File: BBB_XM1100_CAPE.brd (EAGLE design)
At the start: 54.6 x 71.8 mm, 24 parts, among them U2 MIC5225-3.3

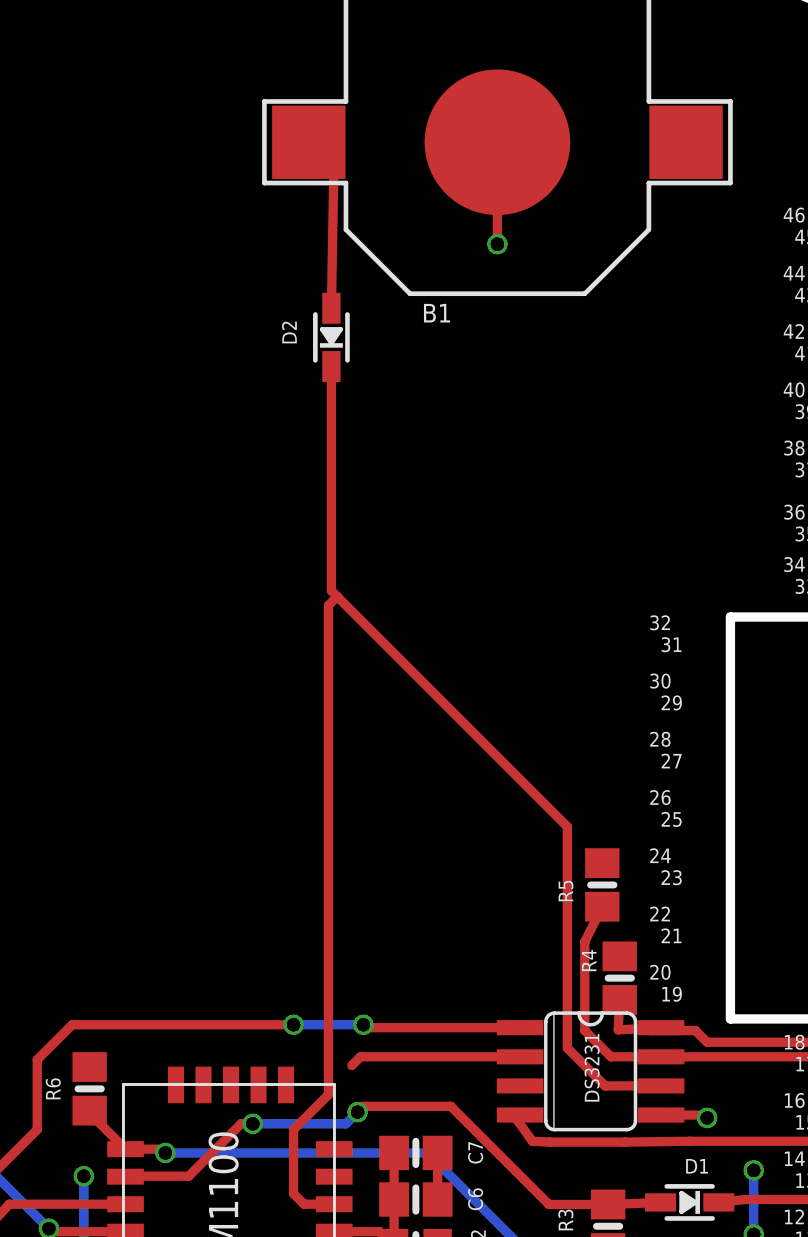
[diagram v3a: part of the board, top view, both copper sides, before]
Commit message: added eeprom to XM1100 cape
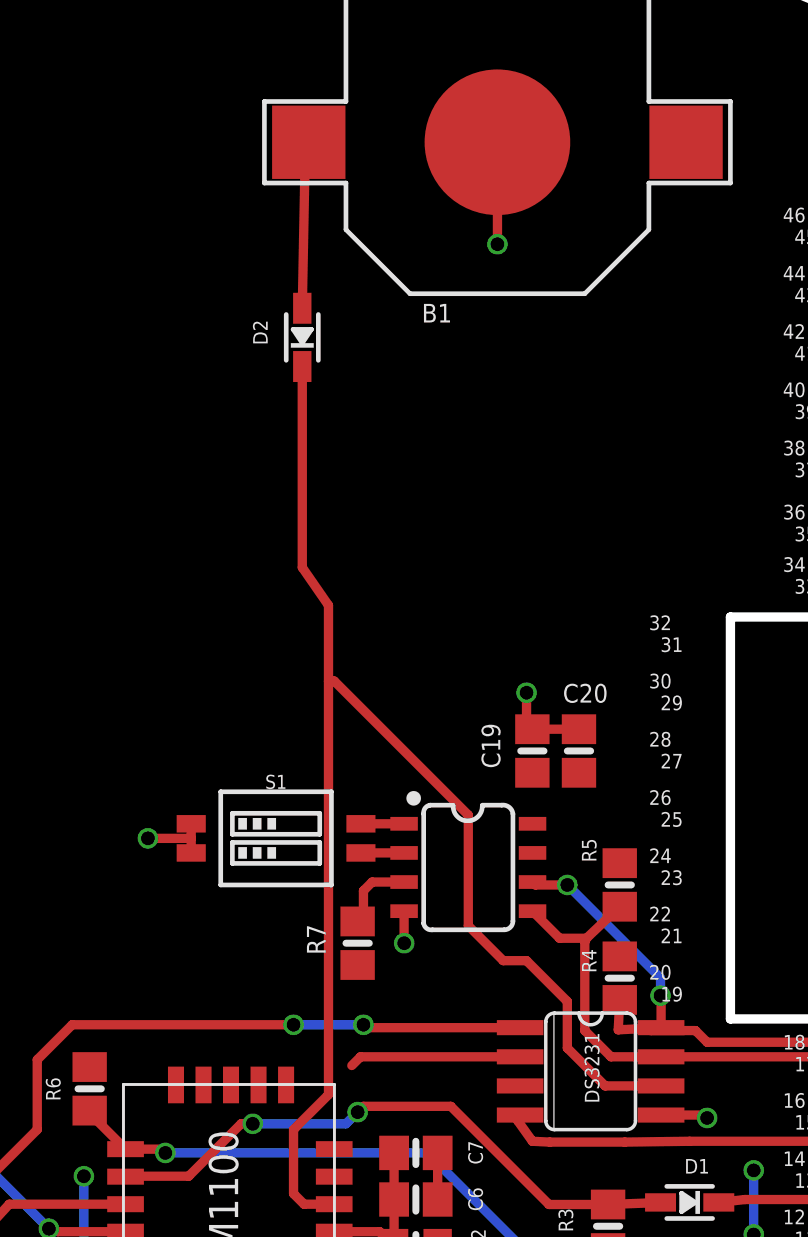
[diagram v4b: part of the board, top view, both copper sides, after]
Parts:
- added C19: 0.1uF, microbuilder:0805-NO
- added C20: 10uF, microbuilder:0805-NO
- added R7: 10K, microbuilder:0805-NO
- added S1: DIP-02-SMD-50MIL, SparkFun-Switches:DIPSWITCH-02-50MIL
- added U1: 24LC256, SparkFun-IC-Memory:SO08
- moved D2 1.27 mm to (27.8, 56.1)
- moved R5 0.76 mm to (41.7, 32.3)
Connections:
- new net N$13: R7.2, U1.3
- new net N$15: S1.3, U1.2
- new net N$16: S1.4, U1.1
- net 3.3V: now also C19.1, C20.1, R7.1, U1.8
- net GND: now also C19.2, C20.2, S1.1, S1.2, U1.4
- net SCL: now also U1.6
- net SDA: now also U1.5
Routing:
- net SCL: track 17.2 -> 26.6 mm, vias 0 -> 2
- net GND: track 17.2 -> 25.5 mm, vias 15 -> 18
- net N$13: track 0.00 -> 3.37 mm
- net SDA: track 18.9 -> 22.2 mm
- net VBACKUP: track 67.5 -> 64.9 mm
- net N$16: track 0.00 -> 1.88 mm
- net N$15: track 0.00 -> 1.88 mm
- net N$1: track 8.35 -> 7.26 mm
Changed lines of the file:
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@@
 </element>
 <element name="U$20" library="microbuilder" package="U.FL" value="U.FL" x="18.288" y="8.255" smashed="yes"/>
-<element name="D2" library="microbuilder" package="SOD-323" value="CUS520" x="29.083" y="56.134" smashed="yes" rot="R90">
-<attribute name="NAME" x="27.575" y="55.796" size="0.635" layer="25" rot="R90"/>
+<element name="D2" library="microbuilder" package="SOD-323" value="CUS520" x="27.813" y="56.134" smashed="yes" rot="R90">
+<attribute name="NAME" x="26.305" y="55.796" size="0.635" layer="25" rot="R90"/>
 </element>
 <element name="U$15" library="adafruit" package="BEAGLEBONE_SHIELD" value="BEAGLEBONE_OUTLINE" x="2.794" y="-14.478" smashed="yes"/>
@@
 <attribute name="NAME" x="40.005" y="29.464" size="0.635" layer="25" rot="R270"/>
 </element>
-<element name="R5" library="microbuilder" package="0805-NO" value="10K" x="40.894" y="32.258" smashed="yes" rot="R270">
-<attribute name="NAME" x="38.989" y="32.512" size="0.635" layer="25" rot="R270"/>
+<element name="R5" library="microbuilder" package="0805-NO" value="10K" x="41.656" y="32.258" smashed="yes" rot="R270">
+<attribute name="NAME" x="40.005" y="34.29" size="0.635" layer="25" rot="R270"/>
 </element>
 <element name="DS3231" library="tuckerLib" package="SO08" value="DS3231M-8PIN" x="40.386" y="24.13" smashed="yes" rot="R270">
@@
 <element name="R6" library="microbuilder" package="0805-NO" value="10K" x="18.542" y="23.368" smashed="yes" rot="R270">
 <attribute name="NAME" x="16.637" y="23.876" size="0.635" layer="25" rot="R270"/>
+</element>
+<element name="U1" library="SparkFun-IC-Memory" package="SO08" value="24LC256" x="35.052" y="33.02" smashed="yes" rot="R270">
+<attribute name="PROD_ID" value="IC-09714" x="44.45" y="33.02" size="1.778" layer="27" rot="R270" display="off"/>
+<attribute name="VALUE" x="35.306" y="32.766" size="0.6096" layer="27" font="vector" ratio="20" rot="R90" align="bottom-center"/>
+</element>
+<element name="S1" library="SparkFun-Switches" package="DIPSWITCH-02-50MIL" value="DIP-02-SMD-50MIL" x="26.67" y="34.29" smashed="yes" rot="R270">
+<attribute name="PROD_ID" value="SWCH-13215" x="28.956" y="40.386" size="1.778" layer="27" rot="R270" display="off"/>
+<attribute name="NAME" x="26.67" y="36.449" size="0.6096" layer="25" font="vector" ratio="20" align="bottom-center"/>
+</element>
+<element name="R7" library="microbuilder" package="0805-NO" value="10K" x="30.226" y="29.718" smashed="yes" rot="R90">
+<attribute name="NAME" x="28.829" y="29.21" size="0.8128" layer="25" ratio="18" rot="R90"/>
+</element>
+<element name="C19" library="microbuilder" package="0805-NO" value="0.1uF" x="37.846" y="38.1" smashed="yes" rot="R90">
+<attribute name="NAME" x="36.449" y="37.338" size="0.8128" layer="25" ratio="18" rot="R90"/>
+</element>
+<element name="C20" library="microbuilder" package="0805-NO" value="10uF" x="39.878" y="38.1" smashed="yes" rot="R90">
+<attribute name="NAME" x="41.148" y="41.021" size="0.8128" layer="25" ratio="18" rot="R180"/>
 </element>
 </elements>
@@
 <via x="36.322" y="60.198" extent="1-16" drill="0.6" shape="square"/>
 <wire x1="36.322" y1="60.198" x2="36.322" y2="64.643" width="0.4064" layer="1"/>
+<contactref element="S1" pad="1"/>
+<contactref element="S1" pad="2"/>
+<contactref element="U1" pad="4"/>
+<contactref element="C19" pad="2"/>
+<contactref element="C20" pad="2"/>
+<via x="21.082" y="34.29" extent="1-16" drill="0.6" shape="square"/>
+<via x="37.592" y="40.64" extent="1-16" drill="0.6" shape="square"/>
+<via x="32.258" y="29.718" extent="1-16" drill="0.6" shape="square"/>
+<wire x1="32.258" y1="29.718" x2="32.252" y2="29.724" width="0.4064" layer="1"/>
+<wire x1="32.252" y1="29.724" x2="32.252" y2="31.115" width="0.4064" layer="1"/>
+<wire x1="39.878" y1="39.05" x2="37.846" y2="39.05" width="0.4064" layer="1"/>
+<wire x1="37.846" y1="39.05" x2="37.592" y2="39.304" width="0.4064" layer="1"/>
+<wire x1="37.592" y1="39.304" x2="37.592" y2="40.64" width="0.4064" layer="1"/>
+<wire x1="22.97" y1="33.655" x2="22.97" y2="34.29" width="0.4064" layer="1"/>
+<wire x1="22.97" y1="34.29" x2="22.97" y2="34.925" width="0.4064" layer="1"/>
+<wire x1="21.082" y1="34.29" x2="22.97" y2="34.29" width="0.4064" layer="1"/>
 <wire x1="29.206" y1="15.938" x2="29.206" y2="19.538" width="0" layer="19" extent="1-1"/>
 <wire x1="25.906" y1="13.138" x2="27.106" y2="13.138" width="0" layer="19" extent="1-1"/>
@@
 <via x="18.288" y="16.002" extent="1-16" drill="0.6" shape="square"/>
 <wire x1="18.288" y1="16.002" x2="18.288" y2="19.558" width="0.4064" layer="16"/>
+<contactref element="R7" pad="1"/>
+<contactref element="C19" pad="1"/>
+<contactref element="C20" pad="1"/>
+<contactref element="U1" pad="8"/>
 </signal>
 <signal name="ENABLE">
@@
 <wire x1="43.4594" y1="23.495" x2="41.021" y2="23.495" width="0.4064" layer="1"/>
 <wire x1="41.021" y1="23.495" x2="39.37" y2="25.146" width="0.4064" layer="1"/>
-<wire x1="39.37" y1="25.146" x2="39.37" y2="34.798" width="0.4064" layer="1"/>
-<wire x1="39.37" y1="34.798" x2="29.337" y2="44.831" width="0.4064" layer="1"/>
 <wire x1="29.206" y1="18.338" x2="27.89" y2="18.338" width="0.4064" layer="1"/>
 <wire x1="27.89" y1="18.338" x2="27.432" y2="18.796" width="0.4064" layer="1"/>
 <wire x1="27.432" y1="18.796" x2="27.432" y2="21.59" width="0.4064" layer="1"/>
 <wire x1="27.432" y1="21.59" x2="28.956" y2="23.114" width="0.4064" layer="1"/>
-<wire x1="28.956" y1="23.114" x2="28.956" y2="44.45" width="0.4064" layer="1"/>
-<wire x1="28.956" y1="44.45" x2="29.337" y2="44.831" width="0.4064" layer="1"/>
-<wire x1="29.083" y1="54.864" x2="29.083" y2="45.085" width="0.4064" layer="1"/>
-<wire x1="29.083" y1="45.085" x2="29.337" y2="44.831" width="0.4064" layer="1"/>
+<wire x1="28.956" y1="23.114" x2="28.956" y2="41.148" width="0.4064" layer="1"/>
+<wire x1="28.956" y1="41.148" x2="28.956" y2="44.45" width="0.4064" layer="1"/>
+<wire x1="28.956" y1="44.45" x2="27.813" y2="46.101" width="0.4064" layer="1"/>
+<wire x1="27.813" y1="54.864" x2="27.813" y2="46.101" width="0.4064" layer="1"/>
+<wire x1="39.37" y1="25.146" x2="39.37" y2="27.178" width="0.4064" layer="1"/>
+<wire x1="39.37" y1="27.178" x2="37.592" y2="28.956" width="0.4064" layer="1"/>
+<wire x1="37.592" y1="28.956" x2="36.576" y2="28.956" width="0.4064" layer="1"/>
+<wire x1="36.576" y1="28.956" x2="35.052" y2="30.48" width="0.4064" layer="1"/>
+<wire x1="35.052" y1="30.48" x2="35.052" y2="35.306" width="0.4064" layer="1"/>
+<wire x1="35.052" y1="35.306" x2="29.21" y2="41.148" width="0.4064" layer="1"/>
+<wire x1="29.21" y1="41.148" x2="28.956" y2="41.148" width="0.4064" layer="1"/>
 </signal>
 <signal name="TX">
@@
 <contactref element="D2" pad="A"/>
 <contactref element="B1" pad="+$1"/>
-<wire x1="28.0966" y1="64.643" x2="29.21" y2="64.643" width="0.4064" layer="1"/>
-<wire x1="29.21" y1="64.643" x2="29.083" y2="57.404" width="0.4064" layer="1"/>
+<wire x1="28.0966" y1="64.643" x2="27.94" y2="64.135" width="0.4064" layer="1"/>
+<wire x1="27.94" y1="64.135" x2="27.813" y2="57.404" width="0.4064" layer="1"/>
 </signal>
 <signal name="VDD_3V3EXP">
@@
 <wire x1="41.275" y1="24.765" x2="40.132" y2="25.908" width="0.4064" layer="1"/>
 <wire x1="40.132" y1="25.908" x2="40.132" y2="29.784" width="0.4064" layer="1"/>
-<wire x1="40.132" y1="29.784" x2="40.894" y2="31.308" width="0.4064" layer="1"/>
+<wire x1="40.132" y1="29.784" x2="40.2072" y2="29.9344" width="0.4064" layer="1"/>
+<contactref element="U1" pad="5"/>
+<wire x1="40.2072" y1="29.9344" x2="41.656" y2="31.308" width="0.4064" layer="1"/>
+<wire x1="37.852" y1="31.115" x2="39.0326" y2="29.9344" width="0.4064" layer="1"/>
+<wire x1="39.0326" y1="29.9344" x2="40.2072" y2="29.9344" width="0.4064" layer="1"/>
 </signal>
 <signal name="SCL">
@@
 <wire x1="44.958" y1="25.908" x2="43.0209" y2="25.908" width="0.4064" layer="1"/>
 <wire x1="43.0209" y1="25.908" x2="42.920975" y2="26.007925" width="0.4064" layer="1"/>
+<contactref element="U1" pad="6"/>
+<wire x1="37.852" y1="32.385" x2="37.979" y2="32.258" width="0.4064" layer="1"/>
+<wire x1="37.979" y1="32.258" x2="39.37" y2="32.258" width="0.4064" layer="1"/>
+<via x="39.37" y="32.258" extent="1-16" drill="0.6" shape="square"/>
+<wire x1="39.37" y1="32.258" x2="43.434" y2="28.194" width="0.4064" layer="16"/>
+<wire x1="43.434" y1="28.194" x2="43.434" y2="27.432" width="0.4064" layer="16"/>
+<via x="43.434" y="27.432" extent="1-16" drill="0.6" shape="square"/>
+<wire x1="43.434" y1="27.432" x2="43.4594" y2="27.4066" width="0.4064" layer="1"/>
+<wire x1="43.4594" y1="27.4066" x2="43.4594" y2="26.035" width="0.4064" layer="1"/>
 </signal>
 <signal name="SQW">
@@
 <wire x1="31.816" y1="18.542" x2="31.816" y2="20.574" width="0.4064" layer="1"/>
 </signal>
+<signal name="N$13">
+<contactref element="U1" pad="3"/>
+<contactref element="R7" pad="2"/>
+<wire x1="30.226" y1="30.668" x2="30.48" y2="30.922" width="0.4064" layer="1"/>
+<wire x1="30.48" y1="30.922" x2="30.48" y2="32.004" width="0.4064" layer="1"/>
+<wire x1="30.48" y1="32.004" x2="30.861" y2="32.385" width="0.4064" layer="1"/>
+<wire x1="30.861" y1="32.385" x2="32.252" y2="32.385" width="0.4064" layer="1"/>
+</signal>
+<signal name="N$15">
+<contactref element="S1" pad="3"/>
+<contactref element="U1" pad="2"/>
+<wire x1="30.37" y1="33.655" x2="32.252" y2="33.655" width="0.4064" layer="1"/>
+</signal>
+<signal name="N$16">
+<contactref element="U1" pad="1"/>
+<contactref element="S1" pad="4"/>
+<wire x1="30.37" y1="34.925" x2="32.252" y2="34.925" width="0.4064" layer="1"/>
+</signal>
 </signals>

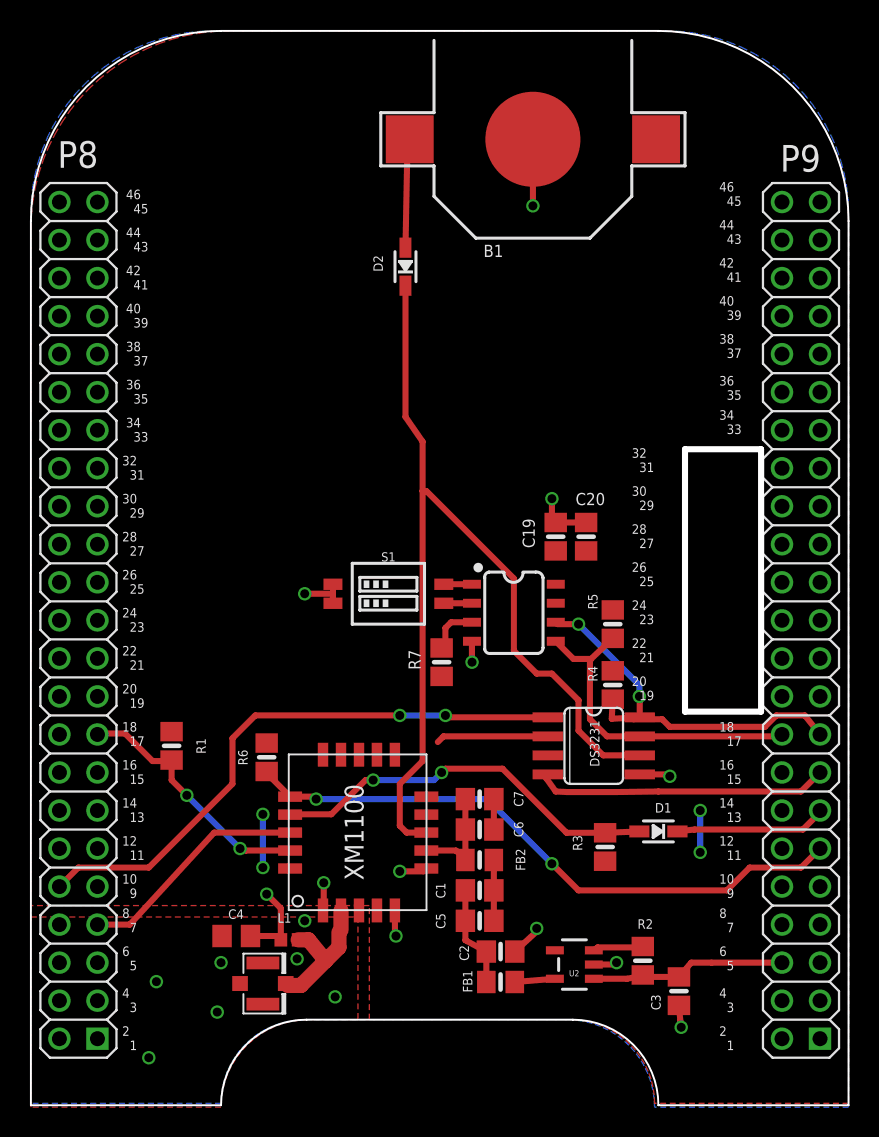
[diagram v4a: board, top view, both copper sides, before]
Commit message: corrected error in VCC/GND connections on xm1100 cape
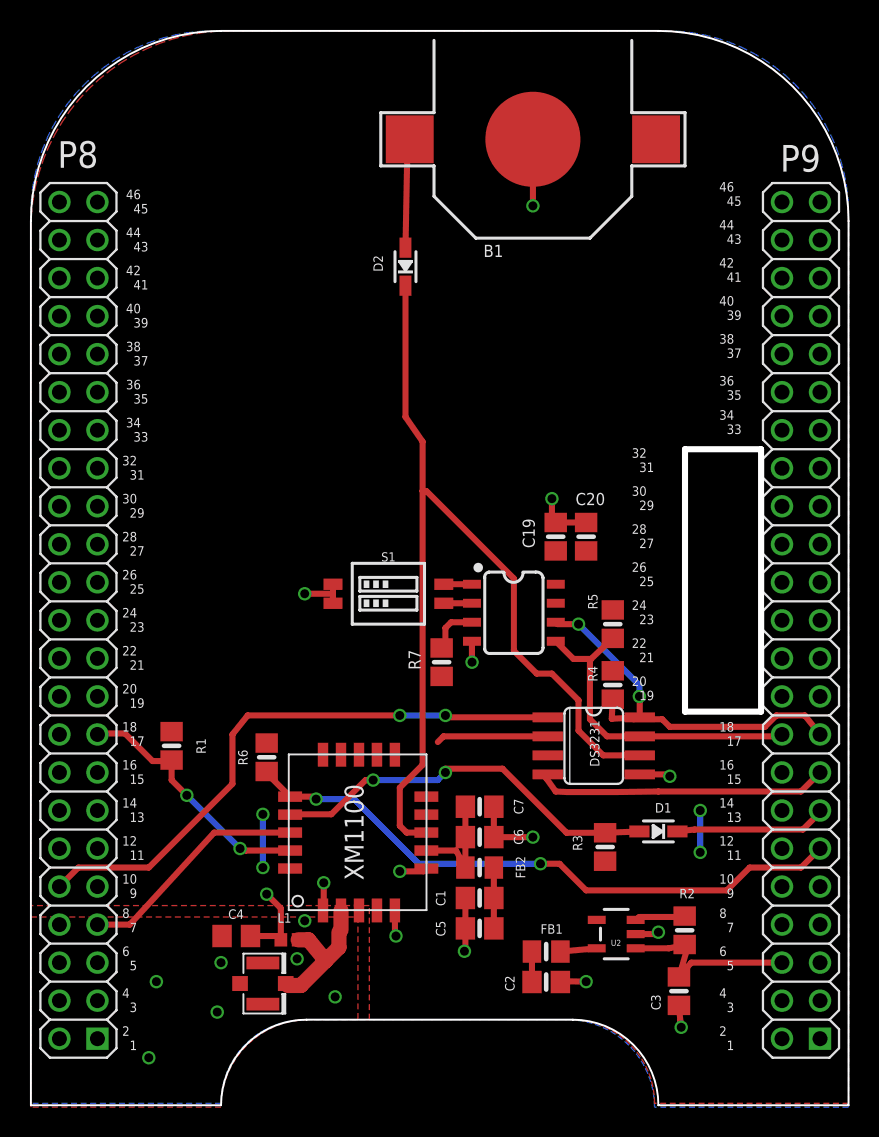
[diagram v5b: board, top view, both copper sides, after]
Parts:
- moved C2 3.66 mm to (37.2, 8.36)
- moved FB1 3.66 mm to (37.2, 10.4)
- moved U2 3.45 mm to (41.9, 11.6)
- moved R2 3.45 mm to (46.5, 11.8)
- moved C6 0.51 mm to (32.8, 18.0)
- moved C7 0.51 mm to (32.8, 20.1)
- moved FB2 0.51 mm to (32.8, 16.0)
- moved C1 0.51 mm to (32.8, 14.0)
- moved C5 0.51 mm to (32.8, 11.9)
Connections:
- removed net N$2: C1.1, C5.1, FB2.1
- net 3.3V: now also C1.1, C5.1, FB2.1; no longer C1.2, C5.2, C6.2, C7.2
- net GND: now also C1.2, C5.2, C6.2, C7.2
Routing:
- net GND: track 25.5 -> 33.2 mm, vias 18 -> 20
- net N$2: track 4.06 -> 0.00 mm
- net 3.3V: track 28.4 -> 25.5 mm
